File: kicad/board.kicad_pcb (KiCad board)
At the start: 2 copper layers, 154.2 x 107.9 mm, 58 parts

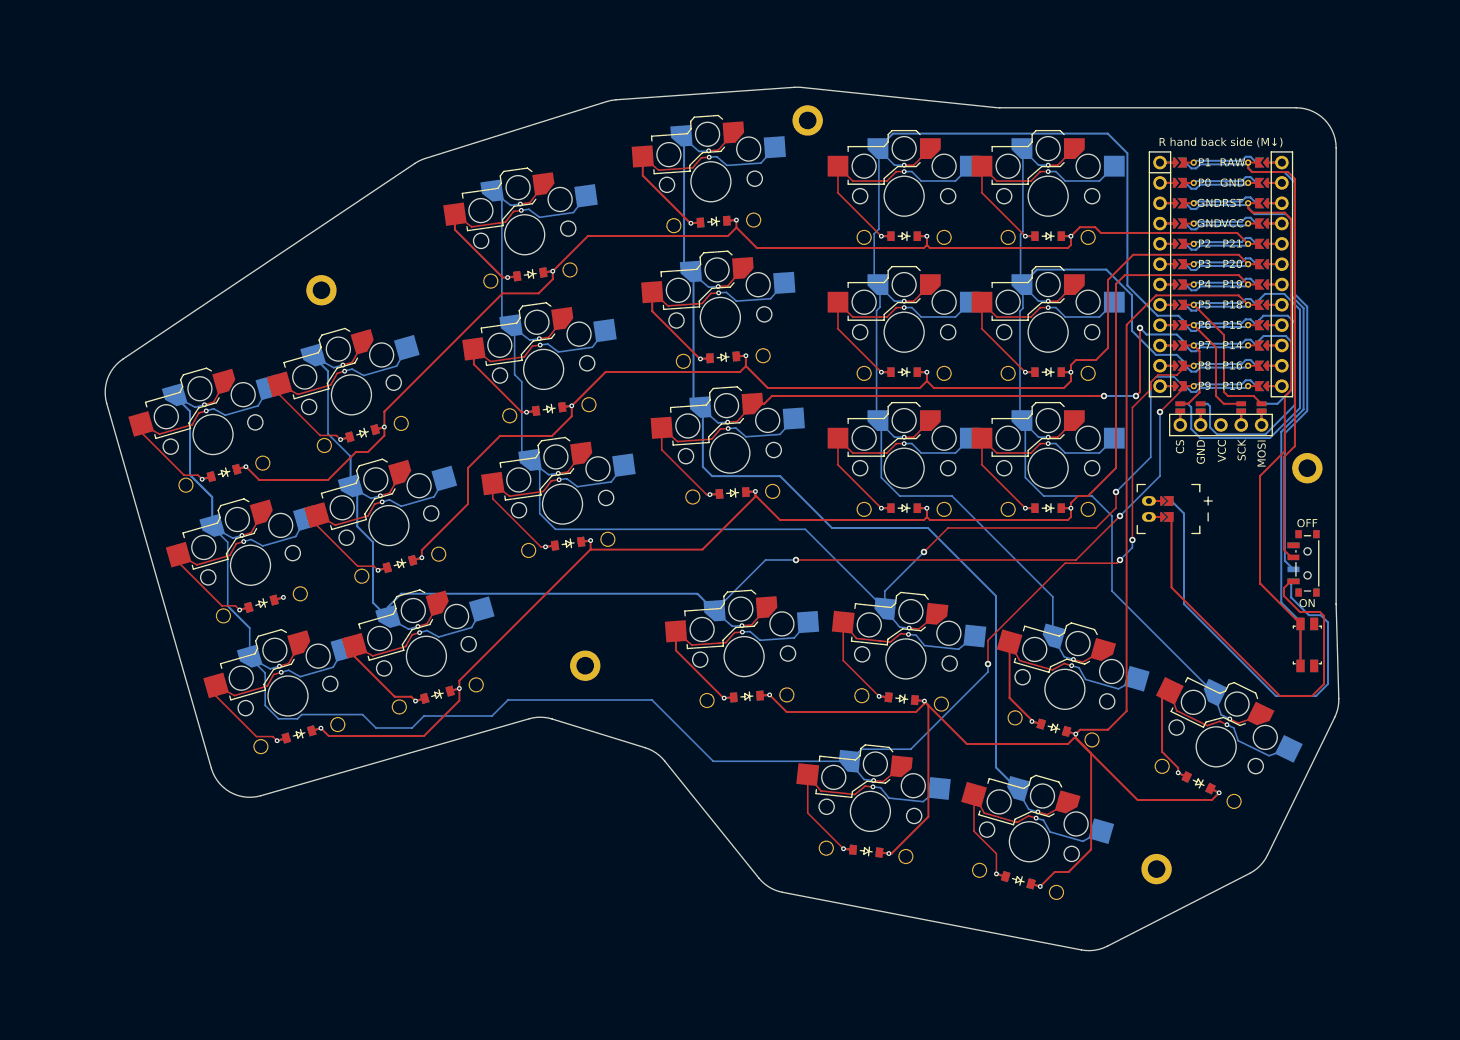
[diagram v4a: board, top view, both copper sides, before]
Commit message: added a ground plane
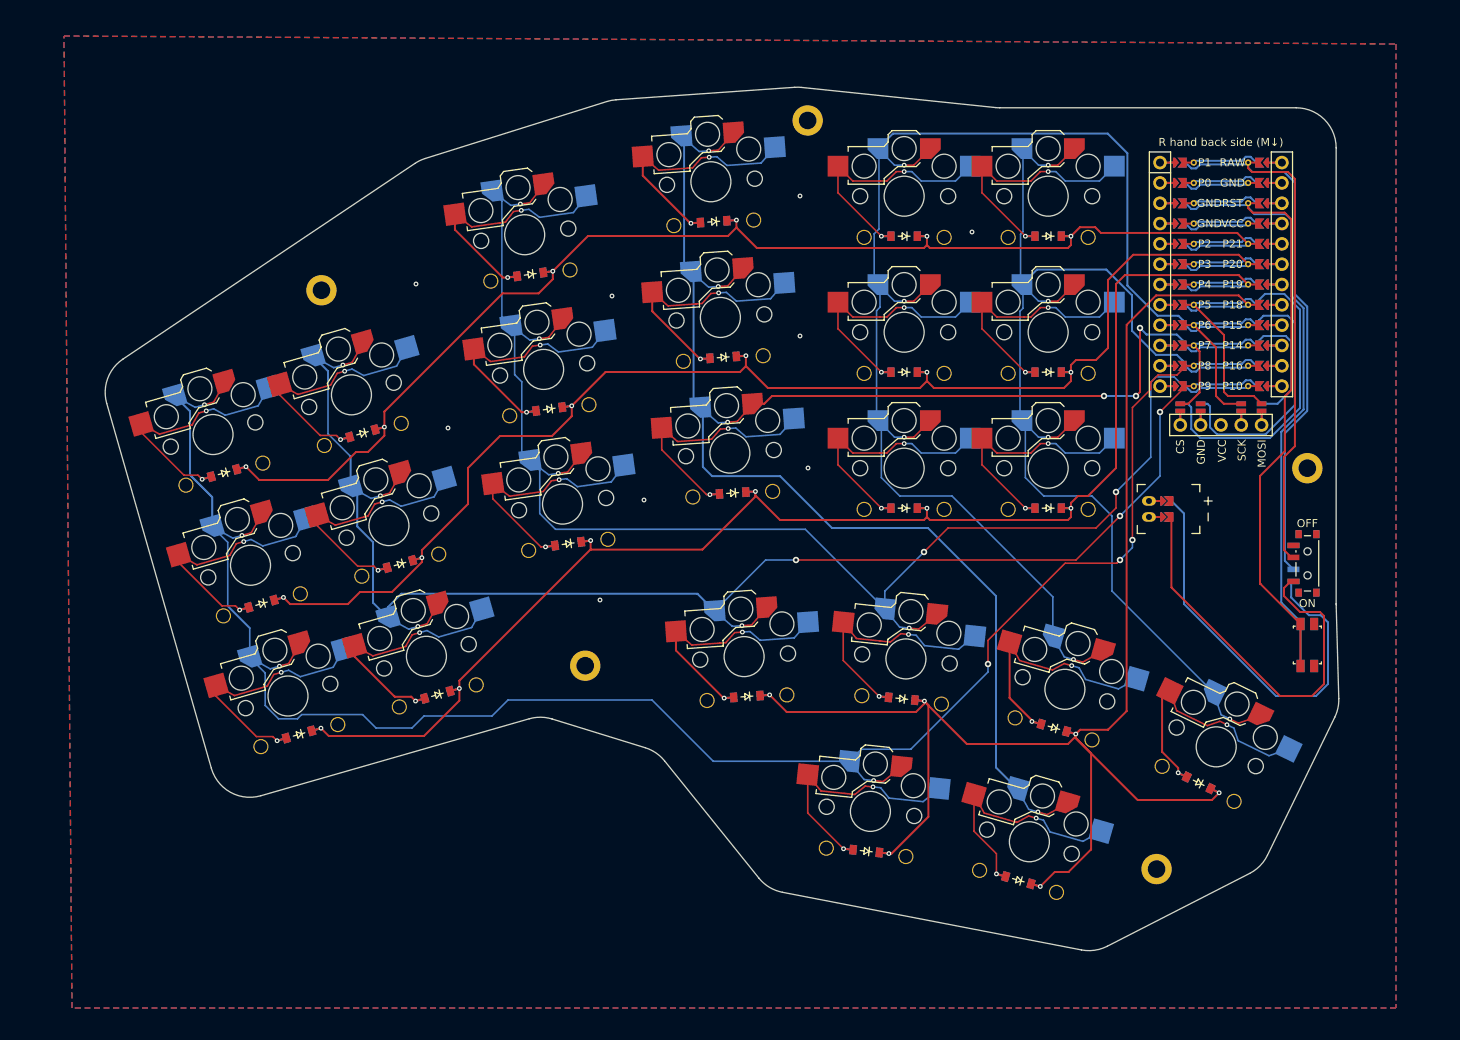
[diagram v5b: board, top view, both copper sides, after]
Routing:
- net P20: track 159.3 -> 179.7 mm
- net P8: track 263.3 -> 256.3 mm
- net GND: vias 0 -> 9
- added copper zone on B.Cu, net GND
- added copper zone on F.Cu, net GND
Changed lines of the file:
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@@
 		(0 "F.Cu" signal)
 		(2 "B.Cu" signal)
-		(9 "F.Adhes" user)
-		(11 "B.Adhes" user)
+		(9 "F.Adhes" user "F.Adhesive")
+		(11 "B.Adhes" user "B.Adhesive")
 		(13 "F.Paste" user)
 		(15 "B.Paste" user)
-		(5 "F.SilkS" user)
-		(7 "B.SilkS" user)
+		(5 "F.SilkS" user "F.Silkscreen")
+		(7 "B.SilkS" user "B.Silkscreen")
 		(1 "F.Mask" user)
 		(3 "B.Mask" user)
-		(17 "Dwgs.User" user)
-		(19 "Cmts.User" user)
-		(21 "Eco1.User" user)
-		(23 "Eco2.User" user)
+		(17 "Dwgs.User" user "User.Drawings")
+		(19 "Cmts.User" user "User.Comments")
+		(21 "Eco1.User" user "User.Eco1")
+		(23 "Eco2.User" user "User.Eco2")
 		(25 "Edge.Cuts" user)
 		(27 "Margin" user)
-		(31 "F.CrtYd" user)
-		(29 "B.CrtYd" user)
+		(31 "F.CrtYd" user "F.Courtyard")
+		(29 "B.CrtYd" user "B.Courtyard")
 		(35 "F.Fab" user)
 		(33 "B.Fab" user)
@@
 		)
 		(pad "2" smd rect
-			(at 8.274999 -3.75 16)
+			(at 8.274998 -3.75 16)
 			(size 2.6 2.6)
 			(layers "B.Cu" "B.Mask" "B.Paste")
@@
 		)
 		(pad "2" smd rect
-			(at 8.274999 -3.75 16)
+			(at 8.274998 -3.75 16)
 			(size 2.6 2.6)
 			(layers "B.Cu" "B.Mask" "B.Paste")
@@
 		)
 		(pad "2" smd rect
-			(at -8.274999 -3.75 344)
+			(at -8.274998 -3.75 344)
 			(size 2.6 2.6)
 			(layers "F.Cu" "F.Mask" "F.Paste")
@@
 		)
 		(pad "2" smd rect
-			(at 8.274999 -3.75 16)
+			(at 8.274998 -3.75 16)
 			(size 2.6 2.6)
 			(layers "B.Cu" "B.Mask" "B.Paste")
@@
 		)
 		(pad "2" smd rect
-			(at 8.274999 -3.75 16)
+			(at 8.274998 -3.75 16)
 			(size 2.6 2.6)
 			(layers "B.Cu" "B.Mask" "B.Paste")
@@
 		)
 		(pad "2" smd rect
-			(at -8.274999 -3.75 344)
+			(at -8.274998 -3.75 344)
 			(size 2.6 2.6)
 			(layers "F.Cu" "F.Mask" "F.Paste")
@@
 		)
 		(pad "2" smd rect
-			(at 8.274999 -3.75 16)
+			(at 8.274998 -3.75 16)
 			(size 2.6 2.6)
 			(layers "B.Cu" "B.Mask" "B.Paste")
@@
 		)
 		(fp_line
-			(start -1.5 -8.200001)
+			(start -1.5 -8.200002)
 			(end -2 -7.7)
 			(stroke
@@
 		(fp_line
 			(start 1.5 -8.2)
-			(end -1.5 -8.200001)
+			(end -1.5 -8.200002)
 			(stroke
 				(width 0.15)
@@
 		)
 		(fp_line
-			(start -1.5 -8.200001)
+			(start -1.5 -8.200002)
 			(end -2 -7.7)
 			(stroke
@@
 		(fp_line
 			(start 1.5 -8.2)
-			(end -1.5 -8.200001)
+			(end -1.5 -8.200002)
 			(stroke
 				(width 0.15)
@@
 		(fp_line
 			(start 2 -7.7)
-			(end 2.000001 -6.78)
+			(end 2.000002 -6.78)
 			(stroke
 				(width 0.15)
@@
 		(fp_line
 			(start 2.52 -6.2)
-			(end 2.000001 -6.78)
+			(end 2.000002 -6.78)
 			(stroke
 				(width 0.15)
@@
 		)
 		(pad "2" smd rect
-			(at 8.274999 -3.75 16)
+			(at 8.274998 -3.75 16)
 			(size 2.6 2.6)
 			(layers "B.Cu" "B.Mask" "B.Paste")
@@
 		)
 		(fp_line
-			(start -1.5 -8.200001)
+			(start -1.5 -8.200002)
 			(end -2 -7.7)
 			(stroke
@@
 		(fp_line
 			(start 1.5 -8.2)
-			(end -1.5 -8.200001)
+			(end -1.5 -8.200002)
 			(stroke
 				(width 0.15)
@@
 		)
 		(fp_line
-			(start -1.5 -8.200001)
+			(start -1.5 -8.200002)
 			(end -2 -7.7)
 			(stroke
@@
 		(fp_line
 			(start 1.5 -8.2)
-			(end -1.5 -8.200001)
+			(end -1.5 -8.200002)
 			(stroke
 				(width 0.15)
@@
 		(fp_line
 			(start 2 -7.7)
-			(end 2.000001 -6.78)
+			(end 2.000002 -6.78)
 			(stroke
 				(width 0.15)
@@
 		(fp_line
 			(start 2.52 -6.2)
-			(end 2.000001 -6.78)
+			(end 2.000002 -6.78)
 			(stroke
 				(width 0.15)
@@
 		)
 		(fp_line
-			(start -1.5 -8.200001)
+			(start -1.5 -8.200002)
 			(end -2 -7.7)
 			(stroke
@@
 		(fp_line
 			(start 1.5 -8.2)
-			(end -1.5 -8.200001)
+			(end -1.5 -8.200002)
 			(stroke
 				(width 0.15)
@@
 		)
 		(fp_line
-			(start -1.5 -8.200001)
+			(start -1.5 -8.200002)
 			(end -2 -7.7)
 			(stroke
@@
 		(fp_line
 			(start 1.5 -8.2)
-			(end -1.5 -8.200001)
+			(end -1.5 -8.200002)
 			(stroke
 				(width 0.15)
@@
 		(fp_line
 			(start 2 -7.7)
-			(end 2.000001 -6.78)
+			(end 2.000002 -6.78)
 			(stroke
 				(width 0.15)
@@
 		(fp_line
 			(start 2.52 -6.2)
-			(end 2.000001 -6.78)
+			(end 2.000002 -6.78)
 			(stroke
 				(width 0.15)
@@
 		(at 222.800641 164.422248 -6)
 		(property "Reference" "S23"
-			(at 0.000001 8.8 354)
+			(at 0.000002 8.8 354)
 			(layer "B.SilkS")
 			(hide yes)
@@
 		(fp_line
 			(start -7 -6.2)
-			(end -2.52 -6.199999)
+			(end -2.52 -6.199998)
 			(stroke
 				(width 0.15)
@@
 		(fp_line
 			(start -2 -6.78)
-			(end -2.52 -6.199999)
+			(end -2.52 -6.199998)
 			(stroke
 				(width 0.15)
@@
 		(fp_line
 			(start 2.52 -6.2)
-			(end 7 -6.200001)
+			(end 7 -6.200002)
 			(stroke
 				(width 0.15)
@@
 		)
 		(fp_line
-			(start 7 -6.200001)
+			(start 7 -6.200002)
 			(end 7 -5.6)
 			(stroke
@@
 		(at 227.242164 145.366003 -6)
 		(property "Reference" "S20"
-			(at 0.000001 8.8 354)
+			(at 0.000002 8.8 354)
 			(layer "B.SilkS")
 			(hide yes)
@@
 		(fp_line
 			(start -7 -6.2)
-			(end -2.52 -6.199999)
+			(end -2.52 -6.199998)
 			(stroke
 				(width 0.15)
@@
 		(fp_line
 			(start -2 -6.78)
-			(end -2.52 -6.199999)
+			(end -2.52 -6.199998)
 			(stroke
 				(width 0.15)
@@
 		(fp_line
 			(start 2.52 -6.2)
-			(end 7 -6.200001)
+			(end 7 -6.200002)
 			(stroke
 				(width 0.15)
@@
 		)
 		(fp_line
-			(start 7 -6.200001)
+			(start 7 -6.200002)
 			(end 7 -5.6)
 			(stroke
@@
 	)
 	(segment
-		(start 137.77733 122.412381)
-		(end 137.77733 115.375118)
-		(width 0.2)
-		(layer "B.Cu")
-		(net 1)
-	)
-	(segment
 		(start 140.525991 125.161042)
 		(end 137.77733 122.412381)
@@
 		(net 3)
 	)
+	(via
+		(at 214 87.5)
+		(size 0.6)
+		(drill 0.3)
+		(layers "F.Cu" "B.Cu")
+		(free yes)
+		(net 3)
+	)
+	(via
+		(at 235.5 92)
+		(size 0.6)
+		(drill 0.3)
+		(layers "F.Cu" "B.Cu")
+		(free yes)
+		(net 3)
+	)
+	(via
+		(at 215 121.5)
+		(size 0.6)
+		(drill 0.3)
+		(layers "F.Cu" "B.Cu")
+		(free yes)
+		(net 3)
+	)
+	(via
+		(at 170 116.5)
+		(size 0.6)
+		(drill 0.3)
+		(layers "F.Cu" "B.Cu")
+		(free yes)
+		(net 3)
+	)
+	(via
+		(at 189 138)
+		(size 0.6)
+		(drill 0.3)
+		(layers "F.Cu" "B.Cu")
+		(free yes)
+		(net 3)
+	)
+	(via
+		(at 190.5 100)
+		(size 0.6)
+		(drill 0.3)
+		(layers "F.Cu" "B.Cu")
+		(free yes)
+		(net 3)
+	)
+	(via
+		(at 214 105)
+		(size 0.6)
+		(drill 0.3)
+		(layers "F.Cu" "B.Cu")
+		(free yes)
+		(net 3)
+	)
+	(via
+		(at 166 98.5)
+		(size 0.6)
+		(drill 0.3)
+		(layers "F.Cu" "B.Cu")
+		(free yes)
+		(net 3)
+	)
+	(via
+		(at 194.5 125.5)
+		(size 0.6)
+		(drill 0.3)
+		(layers "F.Cu" "B.Cu")
+		(free yes)
+		(net 3)
+	)
 	(segment
 		(start 270.318757 90.218529)
@@
 	)
 	(segment
-		(start 142.438165 132.554927)
-		(end 142.5 132.493092)
-		(width 0.25)
-		(layer "F.Cu")
-		(net 4)
-	)
-	(segment
 		(start 142.720999 132.429722)
 		(end 143.52935 130.971418)
@@
 	)
 	(segment
+		(start 149.431948 137.679293)
+		(end 150.259517 138.506862)
+		(width 0.25)
+		(layer "F.Cu")
+		(net 33)
+	)
+	(segment
 		(start 247.868452 108.631548)
 		(end 248.5 108)
@@
 	)
 	(segment
+		(start 150.259517 138.506862)
+		(end 157.493138 138.506862)
+		(width 0.25)
+		(layer "F.Cu")
+		(net 33)
+	)
+	(segment
 		(start 230.736904 111.5)
 		(end 247 111.5)
@@
 	)
 	(segment
+		(start 157.493138 138.506862)
+		(end 159 137)
+		(width 0.25)
+		(layer "F.Cu")
+		(net 33)
+	)
+	(segment
+		(start 163 137)
+		(end 166.734658 133.265342)
+		(width 0.25)
+		(layer "F.Cu")
+		(net 33)
+	)
+	(segment
 		(start 247 111.5)
 		(end 247.868452 110.631548)
@@
 	)
 	(segment
+		(start 159 137)
+		(end 163 137)
+		(width 0.25)
+		(layer "F.Cu")
+		(net 33)
+	)
+	(segment
 		(start 166.717821 132.717821)
 		(end 166.734658 132.717821)
@@
 		(net 33)
 	)
+	(segment
+		(start 166.734658 133.265342)
+		(end 166.734658 132.717821)
+		(width 0.25)
+		(layer "F.Cu")
+		(net 33)
+	)
 	(via
 		(at 247.868452 109.523529)
@@
 		(net 77)
 	)
+	(zone
+		(net 3)
+		(net_name "GND")
+		(layers "F.Cu" "B.Cu")
+		(name "GndPlane")
+		(hatch edge 0.5)
+		(connect_pads
+			(clearance 0)
+		)
+		(min_thickness 0.25)
+		(filled_areas_thickness no)
+		(fill yes
+			(thermal_gap 0.5)
+			(thermal_bridge_width 0.5)
+		)
+		(polygon
+			(pts
+				(xy 288.5 68.5) (xy 288.5 189) (xy 123 189) (xy 122 67.5)
+			)
+		)
+	)
 	(embedded_fonts no)

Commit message: resetting
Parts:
- moved H5 41.3 mm to (278.7, 80.2)
- moved D24 8.34 mm to (233.6, 169.8), turned to 74 degrees
- moved D7 8.34 mm to (176.7, 131.1), turned to 98 degrees
- moved D3 8.34 mm to (133.8, 123.4), turned to 106 degrees
- moved D22 8.34 mm to (256.8, 156.3), turned to 64 degrees
- moved D2 8.34 mm to (138.5, 139.8), turned to 106 degrees
- moved D8 8.34 mm to (174.3, 114.3), turned to 98 degrees
- moved D1 8.34 mm to (143.1, 156.1), turned to 106 degrees
- moved D12 8.34 mm to (194.9, 90.3), turned to 94 degrees
- moved D20 8.34 mm to (218.6, 148.5), turned to 84 degrees
- moved D11 8.34 mm to (196.1, 107.2), turned to 94 degrees
- moved D23 8.34 mm to (214.2, 167.5), turned to 84 degrees
- moved D9 8.34 mm to (171.9, 97.5), turned to 98 degrees
- moved D10 8.34 mm to (197.3, 124.2), turned to 94 degrees
- moved D5 8.34 mm to (155.8, 134.8), turned to 106 degrees
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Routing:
- net (no net): track 0.00 -> 337.7 mm
- net P8: track 256.3 -> 33.1 mm, vias 7 -> 4
- net P18: track 206.6 -> 14.4 mm
- net P14: track 217.5 -> 33.1 mm, vias 7 -> 4
- net P19: track 186.7 -> 14.4 mm
- net P9: track 198.4 -> 33.1 mm, vias 7 -> 4
- net P20: track 179.7 -> 14.4 mm
- net P10: track 191.5 -> 33.1 mm, vias 6 -> 4
- net P21: track 171.6 -> 14.4 mm
- net P15: track 176.5 -> 33.1 mm
- net RST: track 141.2 -> 0.00 mm
- net RAW: track 123.3 -> 0.00 mm
- net P16: track 153.7 -> 33.1 mm
- net BAT_P: track 103.8 -> 0.00 mm
- net MOSI: track 66.6 -> 0.00 mm
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- removed copper zone on B.Cu, net GND
- removed copper zone on F.Cu, net GND
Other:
- board size 154.2 x 107.9 mm -> 155.7 x 107.9 mm
- net class Default added: clearance 0.2, trace_width 0.25, via_dia 0.8, via_drill 0.4

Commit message: coming along quite well
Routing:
- net (no net): track 337.7 -> 0.00 mm
- net P18: track 14.4 -> 195.3 mm
- net P19: track 14.4 -> 188.8 mm
- net P20: track 14.4 -> 182.6 mm
- net P21: track 14.4 -> 175.4 mm
- net P8: track 33.1 -> 166.3 mm
- net P14: track 33.1 -> 153.8 mm
- net P10: track 33.1 -> 133.7 mm
- net P9: track 33.1 -> 123.4 mm
- net P16: track 33.1 -> 121.3 mm
- net P15: track 33.1 -> 116.4 mm
- net BAT_P: track 0.00 -> 40.9 mm, vias 0 -> 2
- net GND: track 0.00 -> 29.5 mm
- net P4: track 0.00 -> 9.84 mm
- net P2: track 0.00 -> 9.84 mm
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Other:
- net class Default removed

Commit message: maybe done?
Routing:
- net P8: track 166.3 -> 248.1 mm, vias 4 -> 7
- net P9: track 123.4 -> 198.6 mm, vias 4 -> 5
- net RST: track 9.83 -> 78.8 mm, vias 0 -> 1
- net VCC: track 9.83 -> 69.1 mm
- net P14: track 153.8 -> 211.9 mm, vias 4 -> 5
- net RAW: track 9.83 -> 65.4 mm, vias 0 -> 1
- net P10: track 133.7 -> 185.0 mm, vias 4 -> 5
- net P15: track 116.4 -> 154.0 mm, vias 4 -> 5
- net MOSI: track 9.84 -> 46.2 mm
- net SCK: track 9.84 -> 39.9 mm
- net GND: track 29.5 -> 54.7 mm, vias 0 -> 29
- net P16: track 121.3 -> 145.6 mm
- net CS: track 9.84 -> 23.3 mm
- added copper zone on B.Cu, net GND
- added copper zone on F.Cu, net GND
